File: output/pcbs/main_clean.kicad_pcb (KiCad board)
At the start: 2 copper layers, 91.2 x 53.1 mm, 19 parts

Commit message: 修复电源开关网络：排针 B+ 改接 BAT_SWITCHED
此前 SuperMini B+ 直连 BAT_PLUS，电池正极绕过开关，开关两焊盘
中 SW OUT（BAT_SWITCHED）为孤立网络。现电路为电池+→SW IN→SW OUT→B+。
README 增补布线与下单流程（ergogen 只布局不布线，须在嘉立创 EDA 布线）。
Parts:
- JST1: footprint JST_PH_S2B-PH-K_02x2.00mm_Angled -> JST_PH_S2B-PH-K_02x2.0mm_Angled
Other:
- outline, holes or cut-outs redrawn
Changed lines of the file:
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@@
       (creategerberjobfile true)
       (excludeedgelayer true)
-      (linewidth 0.100000)
+      (linewidth 0.1)
       (plotframeref false)
       (viasonmask false)
@@
       (hpglpennumber 1)
       (hpglpenspeed 20)
-      (hpglpendiameter 15.000000)
+      (hpglpendiameter 15.0)
       (psnegative false)
       (psa4output false)
@@
             (fp_text value "" (at 0 0) (layer F.SilkS) hide (effects (font (size 1.27 1.27) (thickness 0.15))))
             (pad 1 smd rect (at 0 0 0) (size 1.8 1.8) (layers F.Cu F.Paste F.Mask) (net 5 "KEY_DOWN"))
-(fp_text user 4 DWN P0.20 (at -6.9 0 0) (layer F.SilkS) (effects (font (size 0.8 0.8) (thickness 0.15)) ))
+(fp_text user 4 DWN P0.2 (at -6.9 0 0) (layer F.SilkS) (effects (font (size 0.8 0.8) (thickness 0.15)) ))
             (pad 1 smd rect (at 0 0 0) (size 1.8 1.8) (layers B.Cu B.Paste B.Mask) (net 5 "KEY_DOWN"))
-(fp_text user 4 DWN P0.20 (at -6.9 0 0) (layer B.SilkS) (effects (font (size 0.8 0.8) (thickness 0.15)) (justify mirror)))
+(fp_text user 4 DWN P0.2 (at -6.9 0 0) (layer B.SilkS) (effects (font (size 0.8 0.8) (thickness 0.15)) (justify mirror)))
         )
         (module SMDPad (layer F.Cu)
@@
         )
         (module SMDPad (layer F.Cu)
-            (at 24.130000000000003 14 0)
+            (at 24.13 14 0)
             (fp_text reference "PAD7" (at 0 0) (layer F.SilkS) hide (effects (font (size 1.27 1.27) (thickness 0.15))))
             (fp_text value "" (at 0 0) (layer F.SilkS) hide (effects (font (size 1.27 1.27) (thickness 0.15))))
@@
 (fp_text user 9 B- (at -3.4 0 0) (layer B.SilkS) (effects (font (size 0.8 0.8) (thickness 0.15)) (justify mirror)))
         )
-    (module JST_PH_S2B-PH-K_02x2.00mm_Angled (layer F.Cu)
+    (module JST_PH_S2B-PH-K_02x2.0mm_Angled (layer F.Cu)
         (descr "JST PH series connector, S2B-PH-K, side entry type, through hole, Datasheet: http://www.jst-mfg.com/product/pdf/eng/ePH.pdf")
         (tags "connector jst ph")
@@
 (gr_arc (start 66.675 -19.05) (end 74.175 -19.05) (angle -90) (layer Edge.Cuts) (width 0.15))
 (gr_line (start 66.675 -26.55) (end 47.625 -26.55) (angle 90) (layer Edge.Cuts) (width 0.15))
-(gr_arc (start 47.625 -19.05) (end 47.625 -26.55) (angle -34.16421262093289) (layer Edge.Cuts) (width 0.15))
-(gr_arc (start 38.575 -19.525) (end 43.413250000000005 -25.255736199999998) (angle -40.1731733430704) (layer Edge.Cuts) (width 0.15))
+(gr_arc (start 47.625 -19.05) (end 47.625 -26.55) (angle -34.164213) (layer Edge.Cuts) (width 0.15))
+(gr_arc (start 38.575 -19.525) (end 43.41325 -25.255736) (angle -40.173173) (layer Edge.Cuts) (width 0.15))
 (gr_line (start 36.075 -27.025) (end 38.575 -27.025) (angle 90) (layer Edge.Cuts) (width 0.15))
 (gr_line (start 36.075 -27.025) (end 36.075 -28.575) (angle 90) (layer Edge.Cuts) (width 0.15))
-(gr_arc (start 28.575000000000003 -28.575) (end 36.075 -28.575) (angle -90) (layer Edge.Cuts) (width 0.15))
-(gr_line (start -9.524999999999999 -36.075) (end 28.575000000000003 -36.075) (angle 90) (layer Edge.Cuts) (width 0.15))
-(gr_arc (start -9.524999999999999 -28.575000000000003) (end -9.524999999999999 -36.075) (angle -90) (layer Edge.Cuts) (width 0.15))
-(gr_line (start -17.025 9.524999999999999) (end -17.025 -28.575000000000003) (angle 90) (layer Edge.Cuts) (width 0.15))
-(gr_arc (start -9.525 9.525) (end -17.025 9.525) (angle -90.00000000000003) (layer Edge.Cuts) (width 0.15))
+(gr_arc (start 28.575 -28.575) (end 36.075 -28.575) (angle -90) (layer Edge.Cuts) (width 0.15))
+(gr_line (start -9.525 -36.075) (end 28.575 -36.075) (angle 90) (layer Edge.Cuts) (width 0.15))
+(gr_arc (start -9.525 -28.575) (end -9.525 -36.075) (angle -90) (layer Edge.Cuts) (width 0.15))
+(gr_line (start -17.025 9.525) (end -17.025 -28.575) (angle 90) (layer Edge.Cuts) (width 0.15))
+(gr_arc (start -9.525 9.525) (end -17.025 9.525) (angle -90.0) (layer Edge.Cuts) (width 0.15))
 )

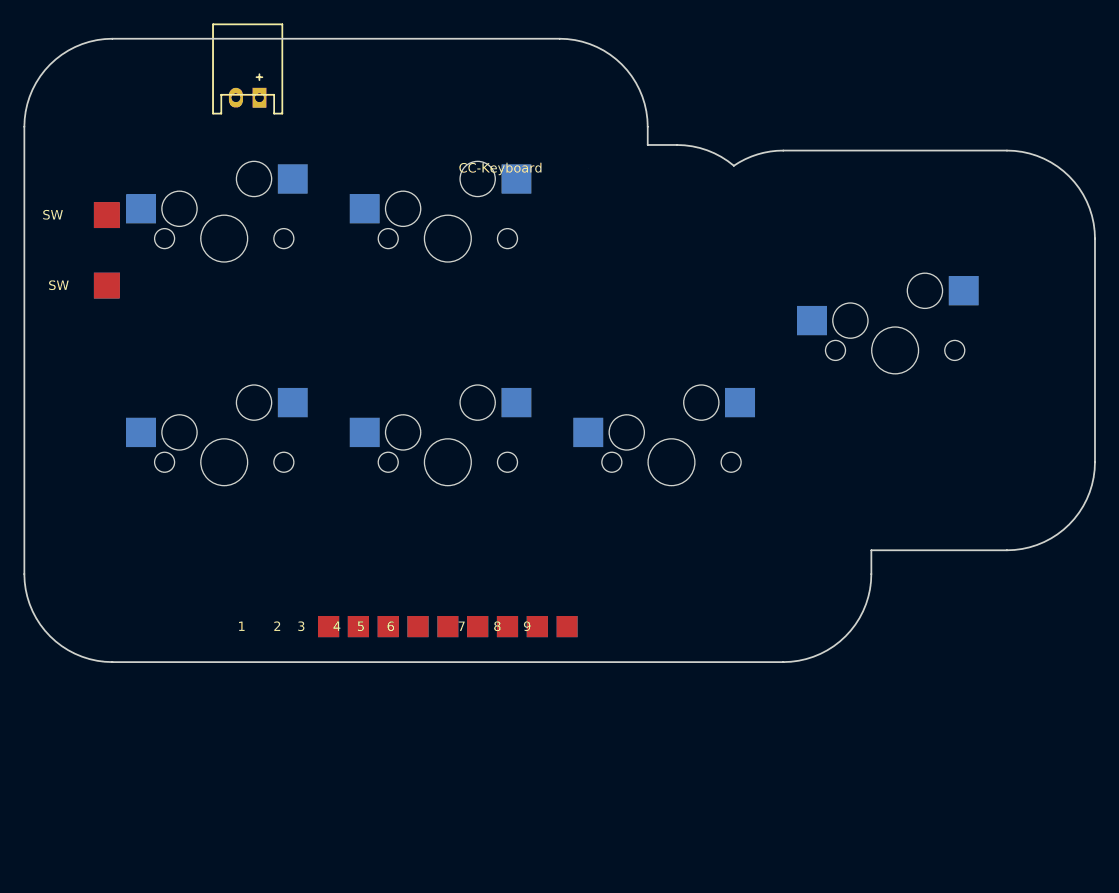
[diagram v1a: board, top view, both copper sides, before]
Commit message: PCB 加底部凸出区：SuperMini 躺平在板上（Pro Micro 兼容排母座）
- 板形加全宽 20mm 凸出区（91.2×70.7mm），定位板仍只含键阵不冲突
- 排母孔按 SuperMini/nice_nano_v2 pinout 摆双排（2.54 网格、排距 15.24），
  仅放用到的 9 孔，行B单孔天然防呆；pinout 经 kriscables 与 nice!nano v2
  两图交叉验证
- 修复：原 pin1-9 用 pad footprint 是贴片焊盘插不了排母，
  postprocess.py 转为 1.0mm 通孔（顺带固化数字规整/SVG 清理）
- 电池 JST、电源开关移入凸出区左右两段
- 接线表/BOM/焊接顺序同步更新
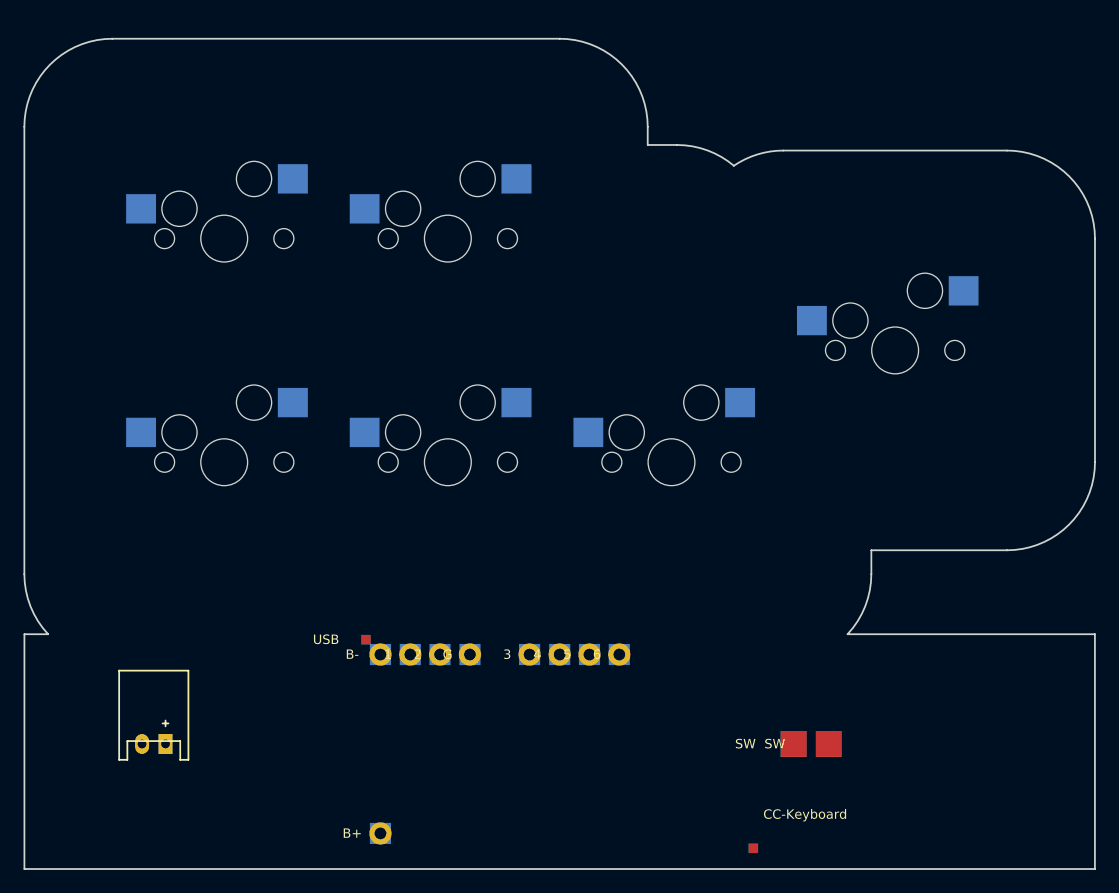
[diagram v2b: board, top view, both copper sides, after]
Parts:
- added PAD13: , SMDPad, F.Cu at (51.5, 24.0)
- added PAD14: , SMDPad, F.Cu at (58.0, 30.0)
- moved PAD11 77.1 mm to (45.1, 32.9)
- moved JST1 55.6 mm to (-6.00, 24.0)
- moved PAD12 52.1 mm to (48.5, 24.0)
- moved PAD10 37.4 mm to (12.1, 15.1)
- moved PAD9 23.7 mm to (13.3, 31.6)
- moved PAD6 7.38 mm to (28.6, 16.4)
- moved PAD7 7.38 mm to (31.1, 16.4)
- moved PAD8 7.38 mm to (33.7, 16.4)
- moved PAD5 7.36 mm to (26.0, 16.4)
- moved PAD1 5.02 mm to (13.3, 16.4)
- moved PAD2 5.02 mm to (15.8, 16.4)
- moved PAD3 5.02 mm to (18.4, 16.4)
- moved PAD4 5.02 mm to (20.9, 16.4)
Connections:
- PAD1 pad 1: KEY_ESC -> BAT_MINUS
- PAD10 pad 1: BAT_PLUS -> (no net)
- PAD11 pad 1: BAT_SWITCHED -> (no net)
- PAD12 pad 1: (no net) -> BAT_PLUS
- PAD2 pad 1: KEY_UP -> KEY_ESC
- PAD3 pad 1: KEY_LEFT -> KEY_UP
- PAD4 pad 1: KEY_DOWN -> GND
- PAD5 pad 1: KEY_RIGHT -> KEY_LEFT
- PAD6 pad 1: KEY_ENTER -> KEY_DOWN
- PAD7 pad 1: GND -> KEY_RIGHT
- PAD8 pad 1: BAT_SWITCHED -> KEY_ENTER
- PAD9 pad 1: BAT_MINUS -> BAT_SWITCHED
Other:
- board size 91.2 x 53.1 mm -> 91.2 x 70.7 mm

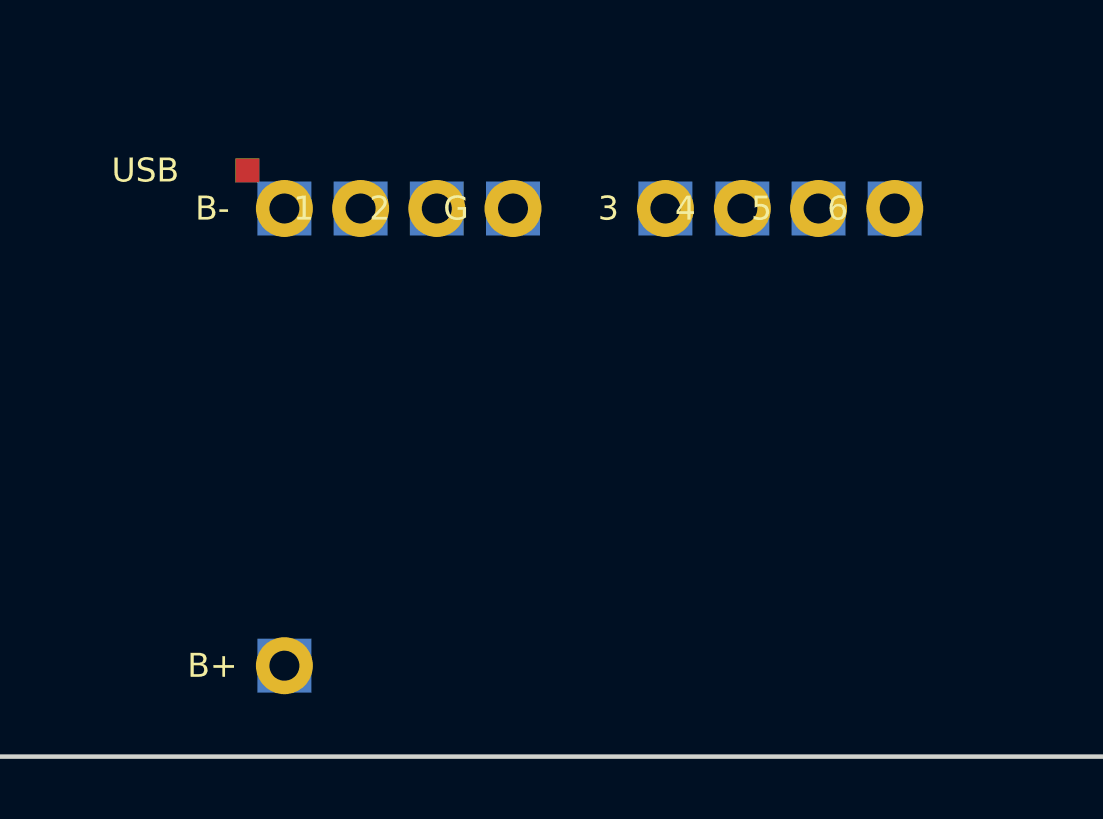
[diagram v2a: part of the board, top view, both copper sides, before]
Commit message: 排母孔位对齐实物 SuperMini（用户提供丝印）
实物每排 12 脚、排距 15.24：行A USB 端起 P0.06 P0.08 GND GND
P0.17 P0.20 P0.22 P0.24 ...（首位不是 B-，与 kriscables 版不同）。
原孔位整体错一格，已重排；该板无独立 B-，电池负极改并入 GND
（BAT_MINUS 网络移除）。行B 单孔 B+ 防呆保留。
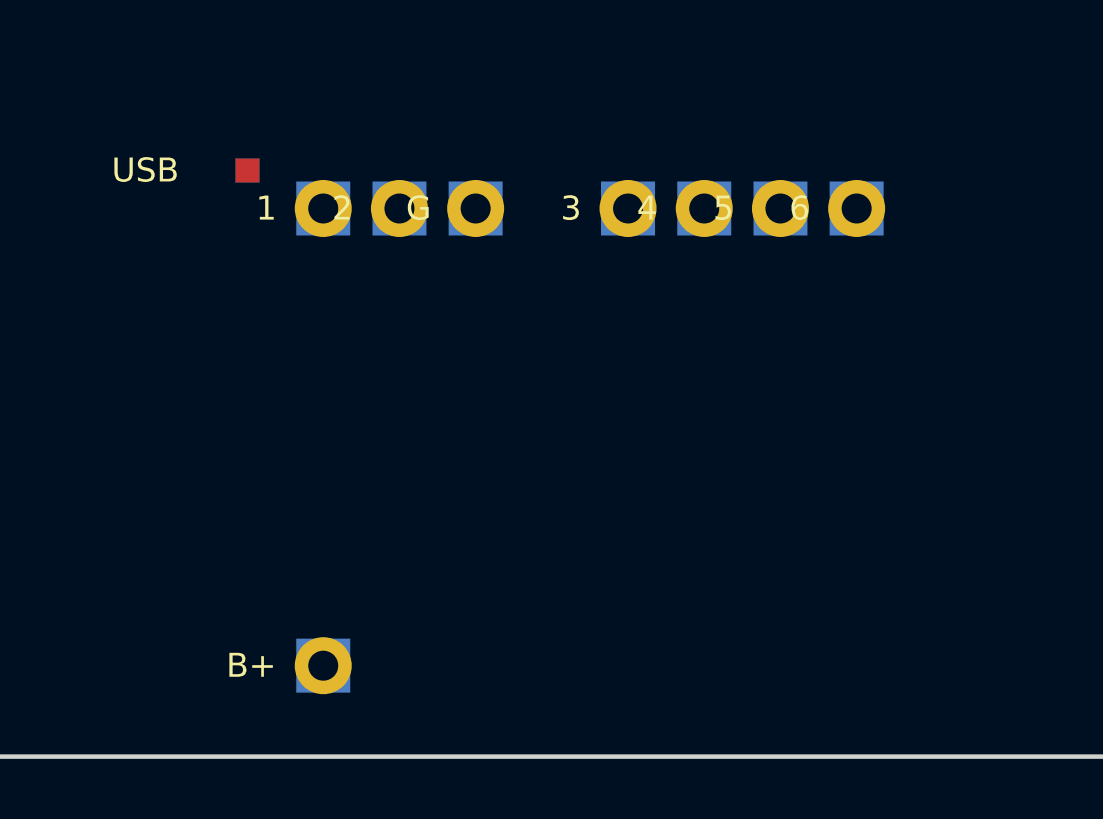
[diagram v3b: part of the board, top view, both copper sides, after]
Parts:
- removed PAD14: , SMDPad
- moved PAD10 37.5 mm to (45.1, 32.9)
- moved PAD8 24.4 mm to (14.6, 31.6)
- moved PAD9 16.6 mm to (12.1, 15.1)
- moved PAD11 9.53 mm to (48.5, 24.0)
- moved PAD13 8.85 mm to (58.0, 30.0)
- moved PAD4 3.84 mm to (24.8, 16.4)
- moved PAD12 3.00 mm to (51.5, 24.0)
- moved PAD1 1.29 mm to (14.6, 16.4)
- moved PAD2 1.29 mm to (17.1, 16.4)
- moved PAD3 1.29 mm to (19.7, 16.4)
- moved PAD5 1.29 mm to (27.3, 16.4)
- moved PAD6 1.27 mm to (29.8, 16.4)
- moved PAD7 1.27 mm to (32.4, 16.4)
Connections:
- JST1 pad 2: BAT_MINUS -> GND
- PAD1 pad 1: BAT_MINUS -> KEY_ESC
- PAD11 pad 1: (no net) -> BAT_PLUS
- PAD12 pad 1: BAT_PLUS -> BAT_SWITCHED
- PAD13 pad 1: BAT_SWITCHED -> (no net)
- PAD2 pad 1: KEY_ESC -> KEY_UP
- PAD3 pad 1: KEY_UP -> GND
- PAD4 pad 1: GND -> KEY_LEFT
- PAD5 pad 1: KEY_LEFT -> KEY_DOWN
- PAD6 pad 1: KEY_DOWN -> KEY_RIGHT
- PAD7 pad 1: KEY_RIGHT -> KEY_ENTER
- PAD8 pad 1: KEY_ENTER -> BAT_SWITCHED
- PAD9 pad 1: BAT_SWITCHED -> (no net)

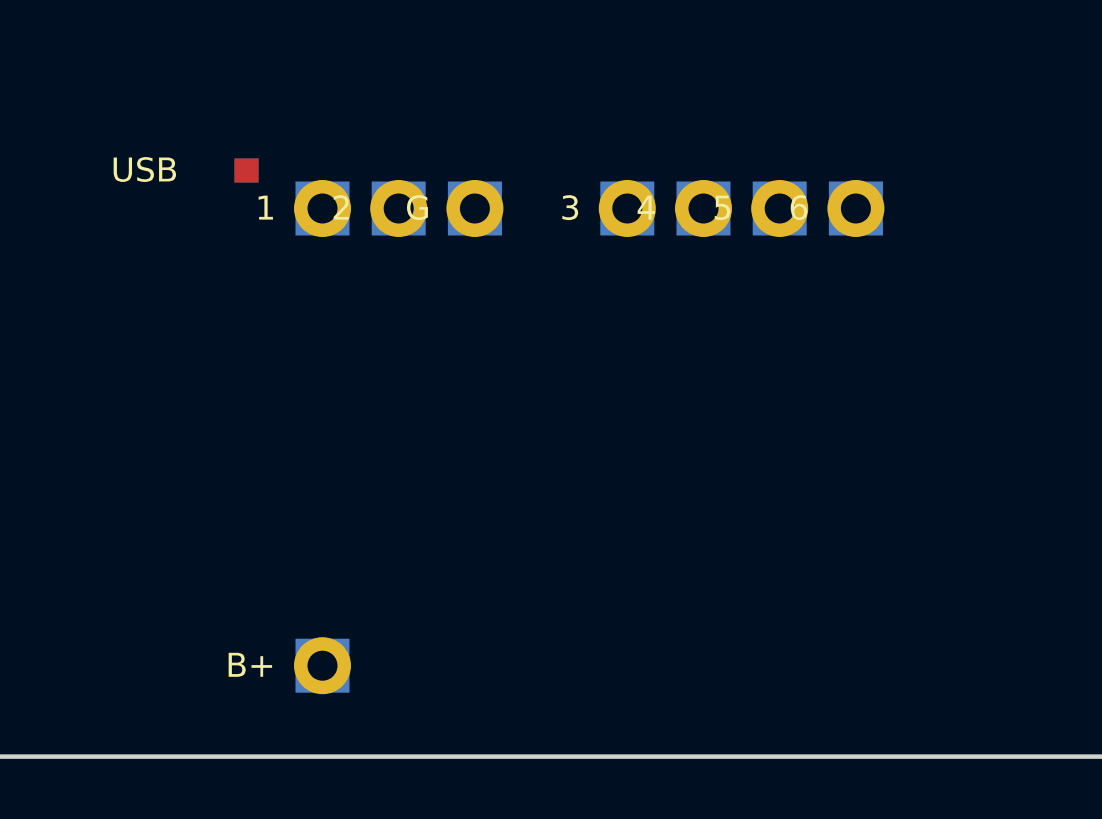
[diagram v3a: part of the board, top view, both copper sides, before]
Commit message: 排母孔位恢复 13×2 布局（用户确认每排 13 脚）
13 孔网格下排 1 首位为 B-（kriscables/nice!nano_v2 两图一致，
用户先前抄丝印漏了最边上的 B-）。B-/B+ 位于板端第一孔位，
BAT_MINUS 网络恢复，电池负极接 B-。
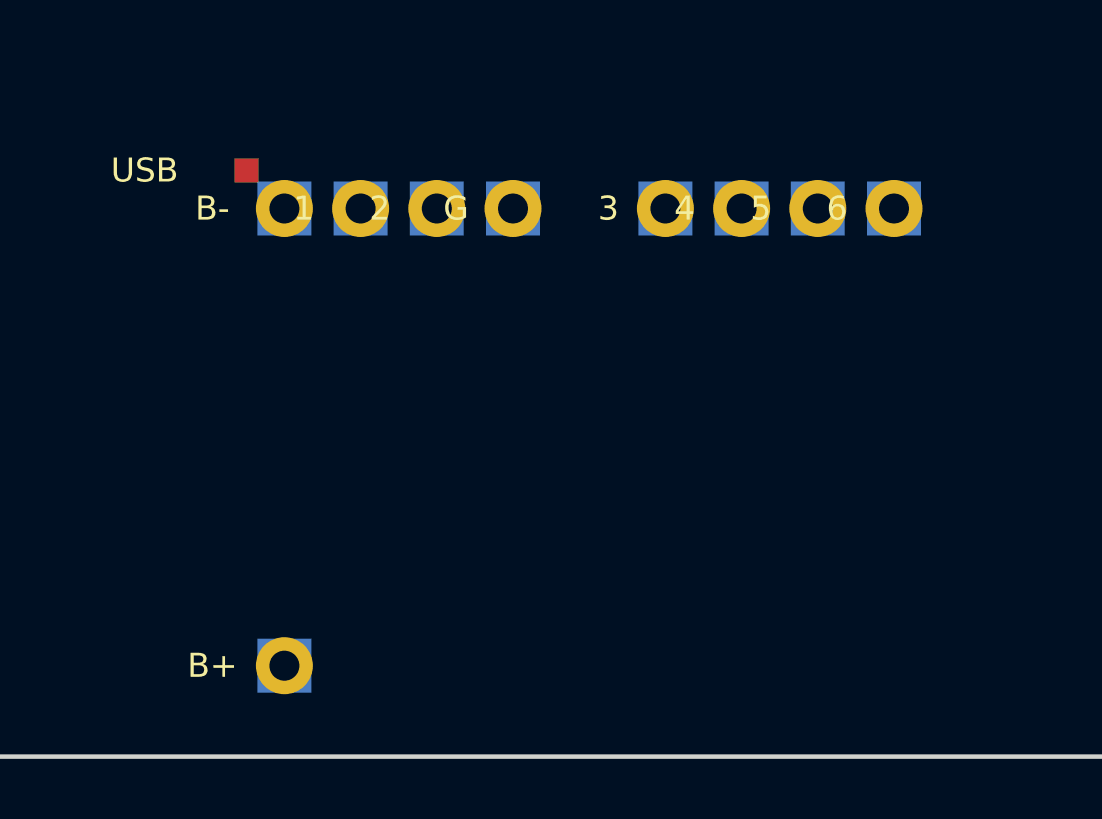
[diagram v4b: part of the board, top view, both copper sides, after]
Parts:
- added PAD14: , SMDPad, F.Cu at (58.0, 30.0)
- moved PAD10 37.5 mm to (12.1, 15.1)
- moved PAD8 24.4 mm to (33.7, 16.4)
- moved PAD9 16.6 mm to (13.3, 31.6)
- moved PAD11 9.53 mm to (45.1, 32.9)
- moved PAD13 8.85 mm to (51.5, 24.0)
- moved PAD4 3.81 mm to (21.0, 16.4)
- moved PAD12 3.00 mm to (48.5, 24.0)
- moved PAD1 1.27 mm to (13.3, 16.4)
- moved PAD2 1.27 mm to (15.9, 16.4)
- moved PAD3 1.27 mm to (18.4, 16.4)
- moved PAD5 1.27 mm to (26.0, 16.4)
- moved PAD6 1.27 mm to (28.6, 16.4)
- moved PAD7 1.27 mm to (31.1, 16.4)
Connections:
- JST1 pad 2: GND -> BAT_MINUS
- PAD1 pad 1: KEY_ESC -> BAT_MINUS
- PAD11 pad 1: BAT_PLUS -> (no net)
- PAD12 pad 1: BAT_SWITCHED -> BAT_PLUS
- PAD13 pad 1: (no net) -> BAT_SWITCHED
- PAD2 pad 1: KEY_UP -> KEY_ESC
- PAD3 pad 1: GND -> KEY_UP
- PAD4 pad 1: KEY_LEFT -> GND
- PAD5 pad 1: KEY_DOWN -> KEY_LEFT
- PAD6 pad 1: KEY_RIGHT -> KEY_DOWN
- PAD7 pad 1: KEY_ENTER -> KEY_RIGHT
- PAD8 pad 1: BAT_SWITCHED -> KEY_ENTER
- PAD9 pad 1: (no net) -> BAT_SWITCHED
